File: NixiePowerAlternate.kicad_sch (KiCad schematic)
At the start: 35 parts, among them J1 12VDC, J2 Screw_Terminal_01x02, J3 Screw_Terminal_01x03, J4 Screw_Terminal_01x03, U1 TPS5430DDA, U2 MAX1771ESA, U3 AMS1117-3.3

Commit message: Add files via upload
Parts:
- added C11: 100uF, Capacitor_Tantalum_SMD:CP_EIA-3528-21_Kemet-B_Pad1.50x2.35mm_HandSolder, symbol Device:C_Polarized_Small_US
- C10: renamed from C13; footprint Capacitor_Tantalum_SMD:CP_EIA-3528-15_AVX-H_Pad1.50x2.35mm_HandSolder -> Capacitor_Tantalum_SMD:CP_EIA-3528-21_Kemet-B_Pad1.50x2.35mm_HandSolder
- C7: value 10uF -> 100uF; footprint Capacitor_Tantalum_SMD:CP_EIA-3216-18_Kemet-A -> Capacitor_Tantalum_SMD:CP_EIA-3528-21_Kemet-B_Pad1.50x2.35mm_HandSolder; LCSC C7171 -> C16133; MPN TAJA106K016RNJ -> TAJB107K006RNJ; Manufacturer Kemet -> Kyocera AVX
- C9: renamed from C8; footprint Capacitor_Tantalum_SMD:CP_EIA-3528-15_AVX-H_Pad1.50x2.35mm_HandSolder -> Capacitor_Tantalum_SMD:CP_EIA-3528-21_Kemet-B_Pad1.50x2.35mm_HandSolder
- D2: value SS14FL -> SS34; footprint Diode_SMD:D_SOD-123F -> Diode_SMD:D_SMA_Handsoldering; LCSC C111580 -> C8678; MPN (none) -> SS34
- L2: footprint (none) -> CoilCraft:L_CoilCraft_MSS1048
- renumbered C5 to C12, C10 to C13, C11 to C14, C4 to C3, C9 to C4, C3 to C5, C12 to C8, J2 to J1, J4 to J2, J1 to J3, J3 to J4, R2 to R1, R3 to R2, R1 to R3, U2 to U1, U3 to U2, U1 to U3
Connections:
- net +5V: now also C11.1
- net GND: now also C11.2
- net +3.3V: no longer names the net of C7.1, J4.2 (Pin_2), U2.2 (VO)

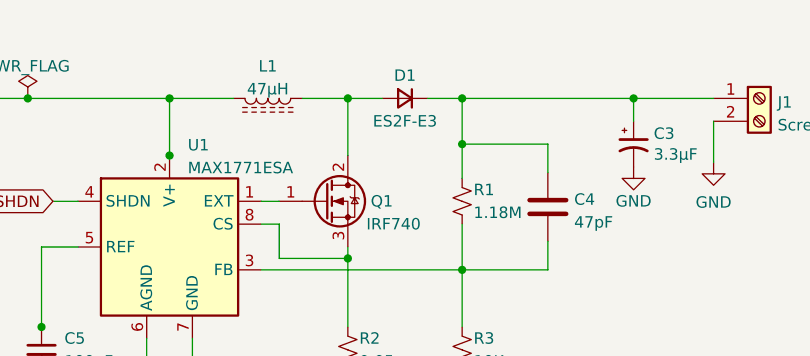
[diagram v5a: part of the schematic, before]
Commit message: Add files via upload
Need to reduce cost before submitting for production.
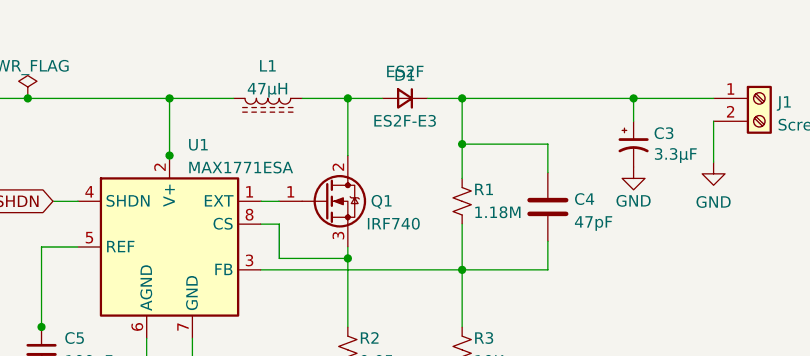
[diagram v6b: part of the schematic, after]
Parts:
- C4: JLCPCB C113890 -> (none); LCSC (none) -> C113890
- D1: value ~ -> ES2F
- R4: LCSC (none) -> C17828
- R5: LCSC (none) -> C245320; MPN (none) -> CR0805F3K24P05Z
- U3: LCSC (none) -> C9864
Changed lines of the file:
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@@
+      (effects (font (size 1.27 1.27)) hide)
+    )
+    (property "LCSC" "C17828" (id 4) (at 187.96 119.38 0)
       (effects (font (size 1.27 1.27)) hide)
     )
@@
     )
     (property "Datasheet" "http://www.ti.com/lit/ds/symlink/tps5430.pdf" (id 3) (at 135.89 118.11 0)
+      (effects (font (size 1.27 1.27)) hide)
+    )
+    (property "LCSC" "C9864" (id 4) (at 135.89 118.11 0)
       (effects (font (size 1.27 1.27)) hide)
     )
@@
     (in_bom yes) (on_board yes)
     (property "Reference" "D1" (id 0) (at 163.83 38.1 0))
-    (property "Value" "~" (id 1) (at 163.83 37.6936 0))
+    (property "Value" "ES2F" (id 1) (at 163.83 37.6936 0))
     (property "Footprint" "Diode_SMD:D_SMB" (id 2) (at 163.83 40.64 90)
       (effects (font (size 1.27 1.27)) hide)
@@
       (effects (font (size 1.27 1.27)) hide)
     )
-    (property "JLCPCB" "C113890" (id 4) (at 179.705 52.705 0)
+    (property "LCSC" "C113890" (id 4) (at 179.705 52.705 0)
       (effects (font (size 1.27 1.27)) hide)
     )
@@
       (effects (font (size 1.27 1.27)) hide)
     )
+    (property "MPN" "CR0805F3K24P05Z" (id 4) (at 187.96 130.81 0)
+      (effects (font (size 1.27 1.27)) hide)
+    )
+    (property "LCSC" "C245320" (id 5) (at 187.96 130.81 0)
+      (effects (font (size 1.27 1.27)) hide)
+    )
     (pin "1")
     (pin "2")
@@
     )
     (path "/b1f04359-6e24-4a92-9d27-0dc0766087e6"
-      (reference "D1") (unit 1) (value "~") (footprint "Diode_SMD:D_SMB")
+      (reference "D1") (unit 1) (value "ES2F") (footprint "Diode_SMD:D_SMB")
     )
     (path "/d32c5515-46f6-4e72-a33f-5545f7212eb8"

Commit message: Add files via upload
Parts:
- C12, C13, C14: value 4.7uF -> 10uF; LCSC C77094 -> C12891; MPN GRM31CR71E475KA88L -> CL31A226KAHNNNE
- C6: value 1uF -> 100nF; LCSC C28323 -> C28233; MPN CL21B105KBFNNNE -> CL21B104KBFNNNE; Manufacturer (none) -> Samsung
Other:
- note added: "C1, C3: low ESR. C3: Optional, see datasheet L1: >3A continuous, ferrite core, shielded. D1: >2A continuous, fast Trr, reverse breakdown >250V. Q1: gate charge <50nC, rDS(ON) <100mOhm."
- note removed: "C1, C4: low ESR. L1: >3A continuous, ferrite core, shielded. D1: >2A continuous, fast Trr, reverse breakdown >250V. Q1: gate charge <50nC, rDS(ON) <100mOhm."
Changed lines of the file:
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@@
 (kicad_sch (version 20211123) (generator eeschema)
   (paper "A4")
+  (title_block
+    (date "2023-02-09")
+    (rev "0.3")
+  )
   (junction (at 101.6 113.03) (diameter 0) (color 0 0 0 0)
   )
@@
     (stroke (width 0) (type default) (color 0 0 0 0))
   )
-  (text "C1, C4: low ESR.\n\nL1: >3A continuous, ferrite core, shielded.\n\nD1: >2A continuous, fast Trr, reverse breakdown >250V.\n\nQ1: gate charge <50nC, rDS(ON) <100mOhm."
+  (text "C1, C3: low ESR.\nC3: Optional, see datasheet\nL1: >3A continuous, ferrite core, shielded.\n\nD1: >2A continuous, fast Trr, reverse breakdown >250V.\n\nQ1: gate charge <50nC, rDS(ON) <100mOhm."
     (at 116.84 97.79 0)
     (effects (font (size 1.27 1.27)) (justify left bottom))
@@
       (effects (font (size 1.27 1.27)) (justify left))
     )
-    (property "Value" "4.7uF" (id 1) (at 93.98 120.6499 0)
+    (property "Value" "10uF" (id 1) (at 93.98 120.6499 0)
       (effects (font (size 1.27 1.27)) (justify left))
     )
@@
       (effects (font (size 1.27 1.27)) hide)
     )
-    (property "MPN" "GRM31CR71E475KA88L" (id 4) (at 90.17 119.38 0)
-      (effects (font (size 1.27 1.27)) hide)
-    )
-    (property "LCSC" "C77094" (id 5) (at 90.17 119.38 0)
+    (property "MPN" "CL31A226KAHNNNE" (id 4) (at 90.17 119.38 0)
+      (effects (font (size 1.27 1.27)) hide)
+    )
+    (property "LCSC" "C12891" (id 5) (at 90.17 119.38 0)
       (effects (font (size 1.27 1.27)) hide)
     )
@@
       (effects (font (size 1.27 1.27)) (justify left))
     )
-    (property "Value" "1uF" (id 1) (at 192.7352 93.853 0)
+    (property "Value" "100nF" (id 1) (at 192.7352 93.853 0)
       (effects (font (size 1.27 1.27)) (justify left))
     )
@@
       (effects (font (size 1.27 1.27)) hide)
     )
-    (property "Manufacturer" "" (id 4) (at 190.5 92.71 0)
-      (effects (font (size 1.27 1.27)) hide)
-    )
-    (property "MPN" "CL21B105KBFNNNE" (id 5) (at 190.5 92.71 0)
-      (effects (font (size 1.27 1.27)) hide)
-    )
-    (property "LCSC" "C28323" (id 6) (at 190.5 92.71 0)
+    (property "Manufacturer" "Samsung" (id 4) (at 190.5 92.71 0)
+      (effects (font (size 1.27 1.27)) hide)
+    )
+    (property "MPN" "CL21B104KBFNNNE" (id 5) (at 190.5 92.71 0)
+      (effects (font (size 1.27 1.27)) hide)
+    )
+    (property "LCSC" "C28233" (id 6) (at 190.5 92.71 0)
       (effects (font (size 1.27 1.27)) hide)
     )
@@
       (effects (font (size 1.27 1.27)) (justify left))
     )
-    (property "Value" "4.7uF" (id 1) (at 105.41 120.6499 0)
+    (property "Value" "10uF" (id 1) (at 105.41 120.6499 0)
       (effects (font (size 1.27 1.27)) (justify left))
     )
@@
       (effects (font (size 1.27 1.27)) hide)
     )
-    (property "MPN" "GRM31CR71E475KA88L" (id 4) (at 101.6 119.38 0)
-      (effects (font (size 1.27 1.27)) hide)
-    )
-    (property "LCSC" "C77094" (id 5) (at 101.6 119.38 0)
+    (property "MPN" "CL31A226KAHNNNE" (id 4) (at 101.6 119.38 0)
+      (effects (font (size 1.27 1.27)) hide)
+    )
+    (property "LCSC" "C12891" (id 5) (at 101.6 119.38 0)
       (effects (font (size 1.27 1.27)) hide)
     )
@@
       (effects (font (size 1.27 1.27)) (justify left))
     )
-    (property "Value" "4.7uF" (id 1) (at 116.84 120.6499 0)
+    (property "Value" "10uF" (id 1) (at 116.84 120.6499 0)
       (effects (font (size 1.27 1.27)) (justify left))
     )
@@
       (effects (font (size 1.27 1.27)) hide)
     )
-    (property "MPN" "GRM31CR71E475KA88L" (id 4) (at 113.03 119.38 0)
-      (effects (font (size 1.27 1.27)) hide)
-    )
-    (property "LCSC" "C77094" (id 5) (at 113.03 119.38 0)
+    (property "MPN" "CL31A226KAHNNNE" (id 4) (at 113.03 119.38 0)
+      (effects (font (size 1.27 1.27)) hide)
+    )
+    (property "LCSC" "C12891" (id 5) (at 113.03 119.38 0)
       (effects (font (size 1.27 1.27)) hide)
     )
@@
     )
     (path "/d125a2a5-cd1e-468e-81d5-207f1c1c1d1c"
-      (reference "C6") (unit 1) (value "1uF") (footprint "Capacitor_SMD:C_0805_2012Metric_Pad1.18x1.45mm_HandSolder")
+      (reference "C6") (unit 1) (value "100nF") (footprint "Capacitor_SMD:C_0805_2012Metric_Pad1.18x1.45mm_HandSolder")
     )
     (path "/da1637f5-e9dd-48a4-9177-ae1e74fbb38c"
@@
     )
     (path "/7ad46cc4-3318-4374-810a-aff6cd741e9c"
-      (reference "C12") (unit 1) (value "4.7uF") (footprint "Capacitor_SMD:C_1206_3216Metric_Pad1.33x1.80mm_HandSolder")
+      (reference "C12") (unit 1) (value "10uF") (footprint "Capacitor_SMD:C_1206_3216Metric_Pad1.33x1.80mm_HandSolder")
     )
     (path "/d72272d9-3fc8-4b0f-a902-c0b5926bc362"
-      (reference "C13") (unit 1) (value "4.7uF") (footprint "Capacitor_SMD:C_1206_3216Metric_Pad1.33x1.80mm_HandSolder")
+      (reference "C13") (unit 1) (value "10uF") (footprint "Capacitor_SMD:C_1206_3216Metric_Pad1.33x1.80mm_HandSolder")
     )
     (path "/e18630e0-6bf2-4de4-bbfe-5ad1aa7d8dfa"
-      (reference "C14") (unit 1) (value "4.7uF") (footprint "Capacitor_SMD:C_1206_3216Metric_Pad1.33x1.80mm_HandSolder")
+      (reference "C14") (unit 1) (value "10uF") (footprint "Capacitor_SMD:C_1206_3216Metric_Pad1.33x1.80mm_HandSolder")
     )
     (path "/b1f04359-6e24-4a92-9d27-0dc0766087e6"

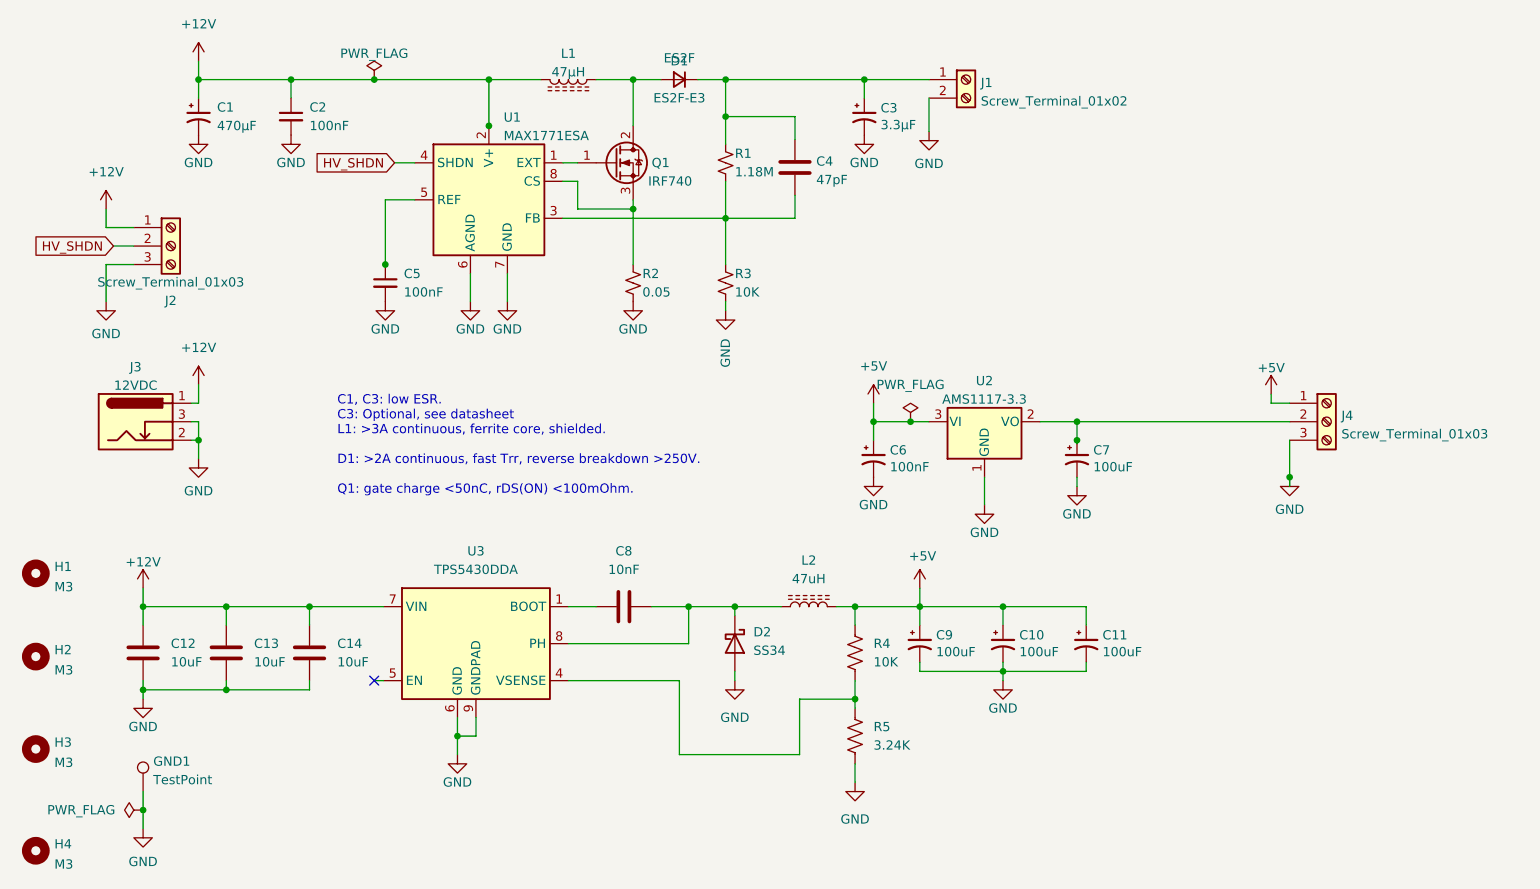
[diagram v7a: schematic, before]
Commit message: Start converting to KiCad 7
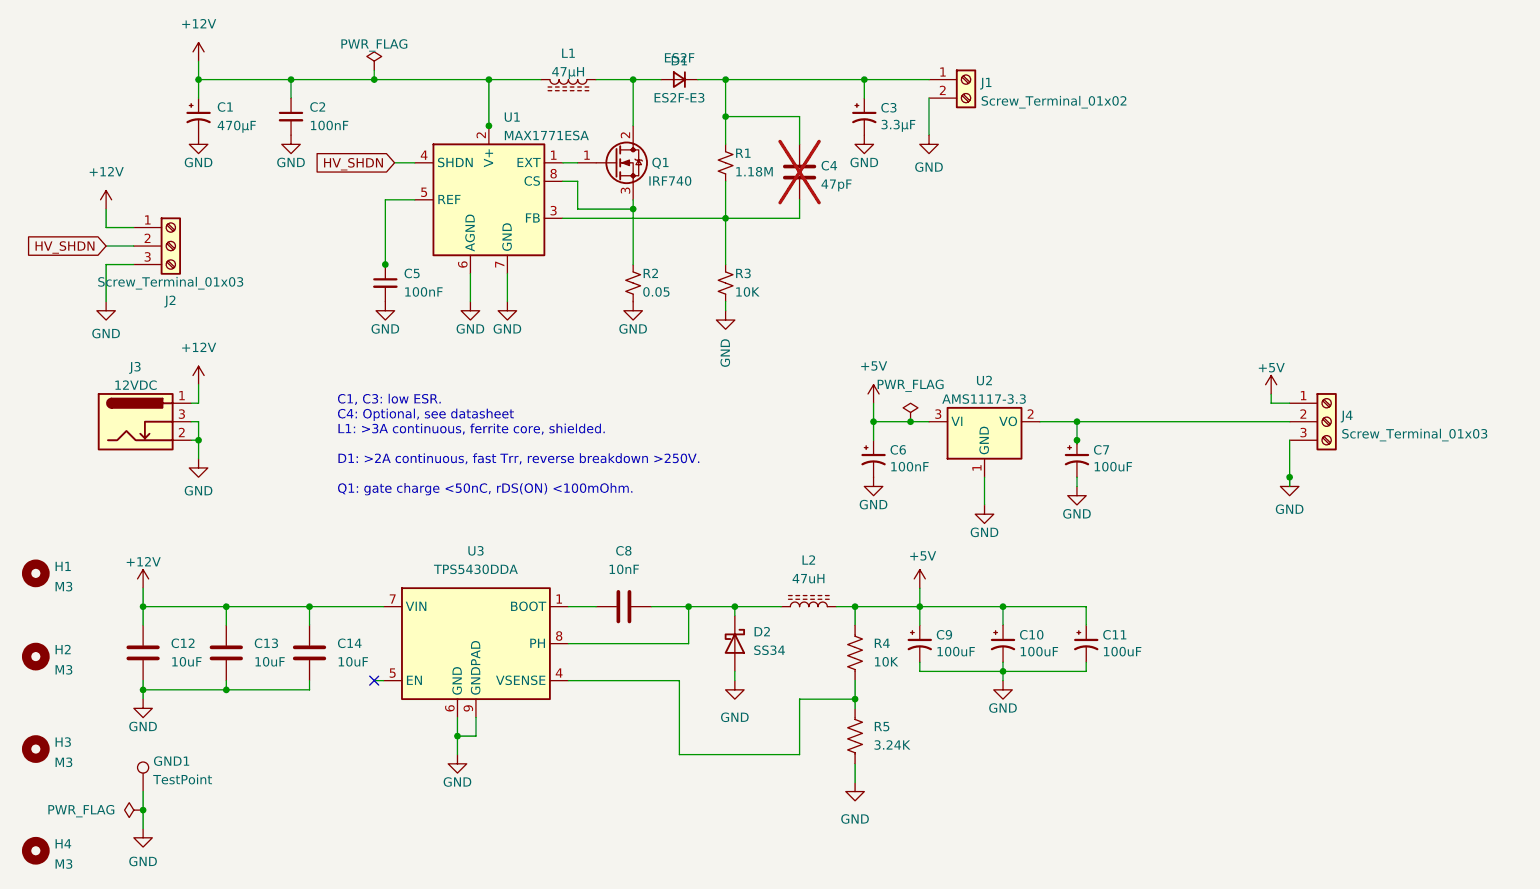
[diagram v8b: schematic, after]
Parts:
- C4: now not fitted
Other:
- note added: "C1, C3: low ESR. C4: Optional, see datasheet L1: >3A continuous, ferrite core, shielded. D1: >2A continuous, fast Trr, reverse breakdown >250V. Q1: gate charge <50nC, rDS(ON) <100mOhm."
- note removed: "C1, C3: low ESR. C3: Optional, see datasheet L1: >3A continuous, ferrite core, shielded. D1: >2A continuous, fast Trr, reverse breakdown >250V. Q1: gate charge <50nC, rDS(ON) <100mOhm."
